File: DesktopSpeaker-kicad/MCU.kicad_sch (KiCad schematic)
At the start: 7 parts, among them J6 SWD, J7 SWD_TC2030, U3 STM32G071RBT6

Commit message: Placement v9: EC11E volume encoder, 25 test points, silkscreen pass (closed sections, border, hole squares, labels), Orwellian logo on back, CAD refit
Co-Authored-By: Claude Sonnet 5.5 <noreply@anthropic.com>
Claude-Session: https://claude.ai/code/session_016fe4xPJbEE2SjGafuyNLjb
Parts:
- added C308, C309, C310: 10nF, DesktopSpeaker:C_0402_1005Metric_Pad0.74x0.62mm_HandSolder, symbol PD_C:PD_C
- added SW102: EC11E, DesktopSpeaker:RotaryEncoder_Alps_EC11E-Switch_Vertical_H20mm_MountingHoles, symbol EC11E_Encoder:EC11E_Encoder
- added TP15: CTRL_SDA, DesktopSpeaker:TestPoint_Keystone_5015_Micro_Mini, symbol TestPoint:TestPoint
- added TP16: CTRL_SCL, DesktopSpeaker:TestPoint_Keystone_5015_Micro_Mini, symbol TestPoint:TestPoint
- added TP17: AUD_SDA, DesktopSpeaker:TestPoint_Keystone_5015_Micro_Mini, symbol TestPoint:TestPoint
- added TP18: AUD_SCL, DesktopSpeaker:TestPoint_Keystone_5015_Micro_Mini, symbol TestPoint:TestPoint
- added TP19: NRST, DesktopSpeaker:TestPoint_Keystone_5015_Micro_Mini, symbol TestPoint:TestPoint
- added TP21: BT_UART_TX, DesktopSpeaker:TestPoint_Keystone_5015_Micro_Mini, symbol TestPoint:TestPoint
- added TP25: GND, DesktopSpeaker:TestPoint_Keystone_5010-5014_Multipurpose, symbol TestPoint:TestPoint
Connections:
- net AUD_SCL: now also TP18.1
- net AUD_SDA: now also TP17.1
- net BT_UART_TX: now also TP21.1
- net CTRL_SCL: now also TP16.1
- net CTRL_SDA: now also TP15.1
- net GND: now also C308.2, C309.2, C310.2, SW102.C, SW102.MP, SW102.S2, TP25.1
- net NRST: now also TP19.1
- net ENC_A: now reaches U3.48 (PC8)
- net ENC_A: now also C308.1, SW102.A
- net ENC_B: now reaches U3.49 (PC9)
- net ENC_B: now also C309.1, SW102.B
- net ENC_SW: now reaches U3.64 (PC10)
- net ENC_SW: now also C310.1, SW102.S1
- no-connect marks 25 -> 22
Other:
- note added: "C, S2 and MP shield to GND."
- note added: "SW102 EC11E encoder + switch (PC8/9/10)"
- note added: "internal pull-ups; 10 nF debounce;"

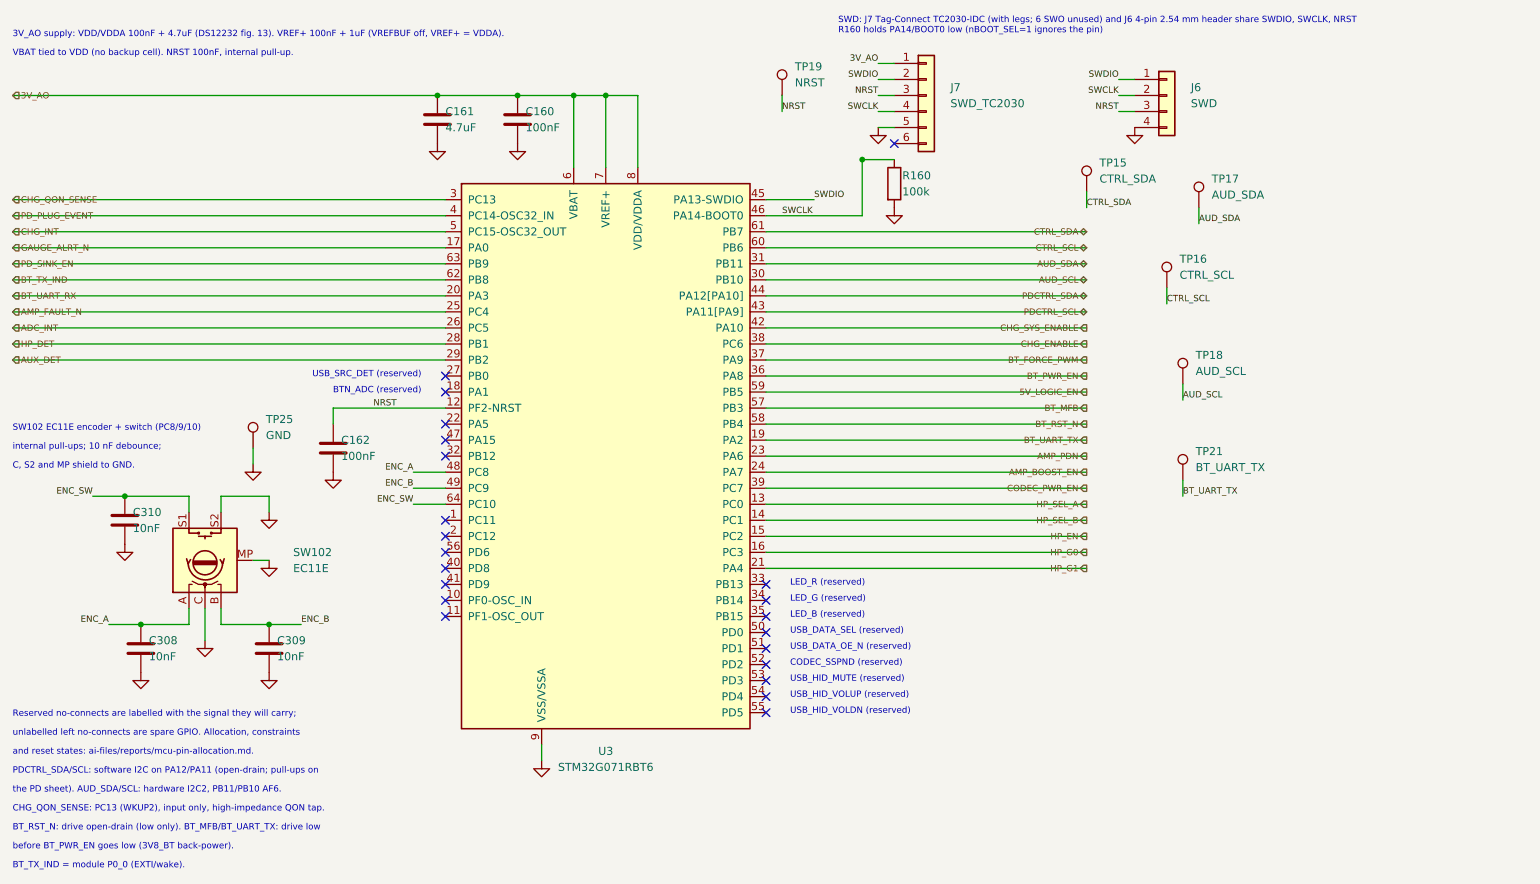
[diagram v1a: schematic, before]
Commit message: Routing R6a-R6m adopted into project board; ERC cleanup, MCU pin swaps, C241 2.2uF, SW100 footprint fix, reviews and helpers
Co-Authored-By: Claude Sonnet 5.5 <noreply@anthropic.com>
Claude-Session: https://claude.ai/code/session_016fe4xPJbEE2SjGafuyNLjb
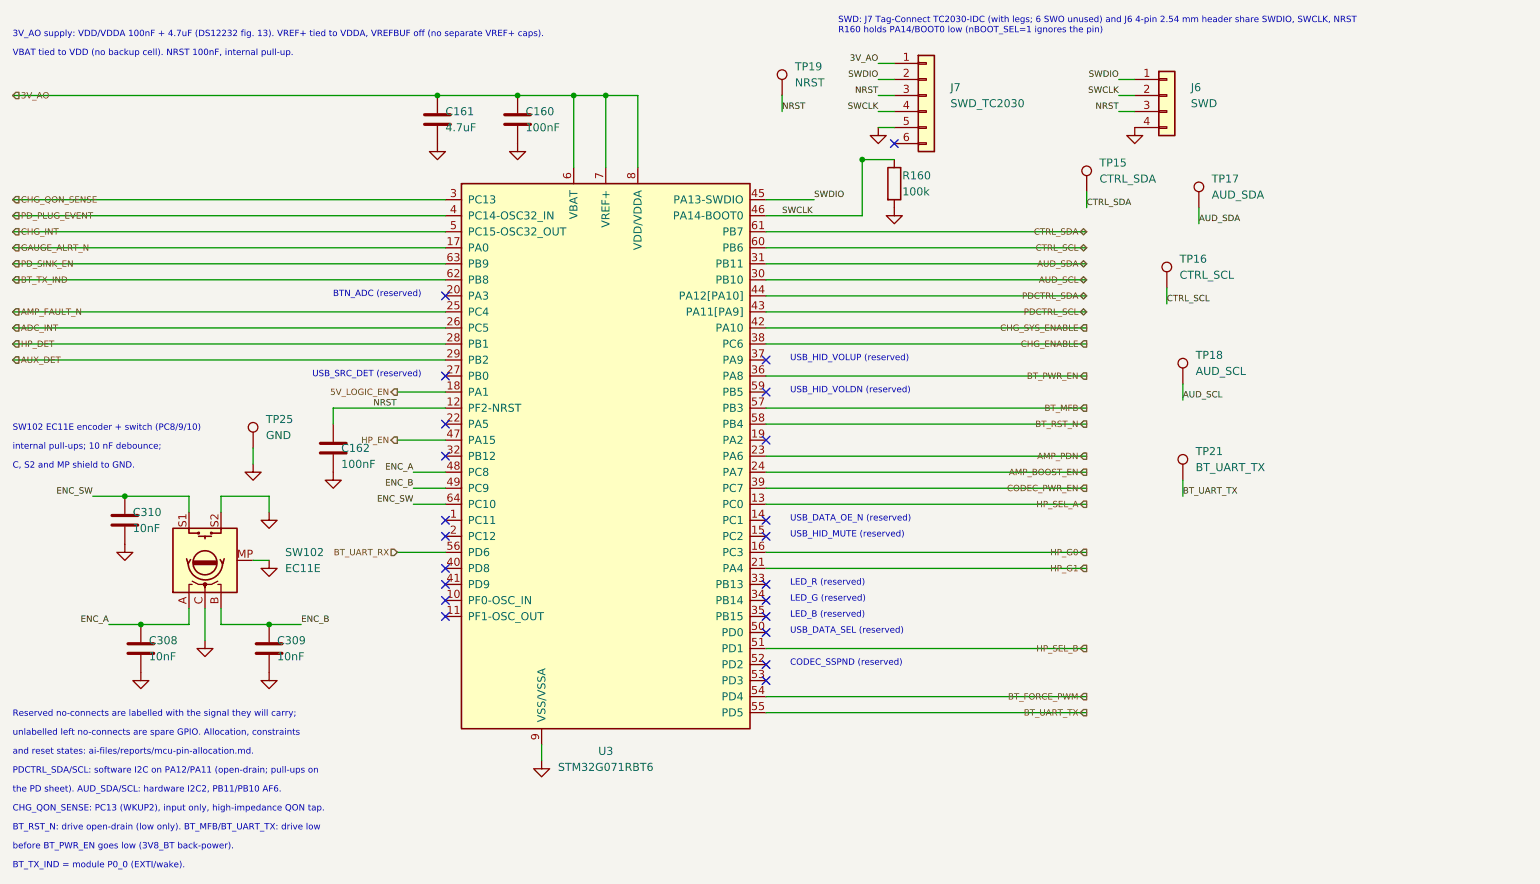
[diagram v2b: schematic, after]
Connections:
- net 5V_LOGIC_EN: now also U3.18 (PA1); no longer U3.59 (PB5)
- net BT_FORCE_PWM: now also U3.54 (PD4); no longer U3.37 (PA9)
- net BT_UART_RX: now also U3.56 (PD6); no longer U3.20 (PA3)
- net BT_UART_TX: now also U3.55 (PD5); no longer U3.19 (PA2)
- net HP_EN: now also U3.47 (PA15); no longer U3.15 (PC2)
- net HP_SEL_B: now also U3.51 (PD1); no longer U3.14 (PC1)
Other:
- note added: "3V_AO supply: VDD/VDDA 100nF + 4.7uF (DS12232 fig. 13). VREF+ tied to VDDA, VREFBUF off (no separate VREF+ caps)."
- note removed: "3V_AO supply: VDD/VDDA 100nF + 4.7uF (DS12232 fig. 13). VREF+ 100nF + 1uF (VREFBUF off, VREF+ = VDDA)."

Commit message: Y200 24.576 MHz crystal with 15 pF load caps, C275 3D model, schematic/PCB sourcing fields synced to BOM
Co-Authored-By: Claude Sonnet 5.5 <noreply@anthropic.com>
Claude-Session: https://claude.ai/code/session_016fe4xPJbEE2SjGafuyNLjb
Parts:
- C161: LCSC (none) -> C1779
- C308, C309, C310: LCSC unverified -> C77019
- SW102: LCSC unverified -> C370970

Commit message: Part substitutions from the sourcing pass: SW102 -> Alps EC11E18244AU (C202365, in stock), SW101 -> CW GRB112B802BR1 (Digi-Key, 20 A/14 VDC); sourcing report and Alps EC11E catalog
Co-Authored-By: Claude Fable 5.1 <noreply@anthropic.com>
Claude-Session: https://claude.ai/code/session_016fe4xPJbEE2SjGafuyNLjb
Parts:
- SW102: LCSC C370970 -> C202365; MPN EC11E15244G1 -> EC11E18244AU
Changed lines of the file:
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@@
 (wire (pts (xy 114.3 130.81) (xy 109.22 130.81)) (stroke (width 0) (type default)))
 (label "ENC_SW" (at 109.22 130.81 0) (effects (font (size 1 1)) (justify right bottom)))
-(symbol (lib_id "EC11E_Encoder:EC11E_Encoder") (at 76.2 139.7 90) (unit 1) (exclude_from_sim no) (in_bom yes) (on_board yes) (dnp no) (property "Reference" "SW102" (at 88.9 138.43 270) (effects (font (size 1.27 1.27)) (justify left))) (property "Value" "EC11E" (at 88.9 140.97 270) (effects (font (size 1.27 1.27)) (justify left))) (property "Footprint" "DesktopSpeaker:RotaryEncoder_Alps_EC11E-Switch_Vertical_H20mm_MountingHoles" (at 76.2 139.7 0) (hide yes) (effects (font (size 1.27 1.27)))) (property "Datasheet" "" (at 76.2 139.7 0) (hide yes) (effects (font (size 1.27 1.27)))) (property "Manufacturer" "Alps Alpine" (at 76.2 139.7 0) (hide yes) (effects (font (size 1 1)))) (property "MPN" "EC11E15244G1" (at 76.2 139.7 0) (hide yes) (effects (font (size 1 1)))) (property "LCSC" "C370970" (at 76.2 139.7 0) (hide yes) (effects (font (size 1 1)))) (pin "A") (pin "B") (pin "C") (pin "S1") (pin "S2") (pin "MP") (instances (project "DesktopSpeaker" (path "/feda53ed-537d-4f88-9436-c6075776255b/4ab2b160-efba-45d8-be2c-c7b2862cfacf" (reference "SW102") (unit 1)))))
+(symbol (lib_id "EC11E_Encoder:EC11E_Encoder") (at 76.2 139.7 90) (unit 1) (exclude_from_sim no) (in_bom yes) (on_board yes) (dnp no) (property "Reference" "SW102" (at 88.9 138.43 270) (effects (font (size 1.27 1.27)) (justify left))) (property "Value" "EC11E" (at 88.9 140.97 270) (effects (font (size 1.27 1.27)) (justify left))) (property "Footprint" "DesktopSpeaker:RotaryEncoder_Alps_EC11E-Switch_Vertical_H20mm_MountingHoles" (at 76.2 139.7 0) (hide yes) (effects (font (size 1.27 1.27)))) (property "Datasheet" "../ai-files/datasheets/Alps_EC11E.pdf" (at 76.2 139.7 0) (hide yes) (effects (font (size 1.27 1.27)))) (property "Manufacturer" "Alps Alpine" (at 76.2 139.7 0) (hide yes) (effects (font (size 1 1)))) (property "MPN" "EC11E18244AU" (at 76.2 139.7 0) (hide yes) (effects (font (size 1 1)))) (property "LCSC" "C202365" (at 76.2 139.7 0) (hide yes) (effects (font (size 1 1)))) (pin "A") (pin "B") (pin "C") (pin "S1") (pin "S2") (pin "MP") (instances (project "DesktopSpeaker" (path "/feda53ed-537d-4f88-9436-c6075776255b/4ab2b160-efba-45d8-be2c-c7b2862cfacf" (reference "SW102") (unit 1)))))
 (wire (pts (xy 73.66 147.32) (xy 73.66 149.86)) (stroke (width 0) (type default)))
 (wire (pts (xy 73.66 149.86) (xy 60.96 149.86)) (stroke (width 0) (type default)))
